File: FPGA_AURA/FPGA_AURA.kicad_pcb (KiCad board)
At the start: 8 copper layers, 50 x 50 mm, 187 parts, among them J1 ST5-40-1.00-L-D-P-TR, J100 USB_C_Receptacle_USB2.0_16P, J101 XT30PW-M, U1 XC7A35T-2FTG256C, U2 W25Q256JVEIQ, U200 ADP5014, U3 FT2232HQ, U4 TPS51200DRCR, U5 USBLC6-2SC6, U500 MT41K128M16JT-125_IT_K, U6 93LC56BT-I_SN, Y1 12MHz

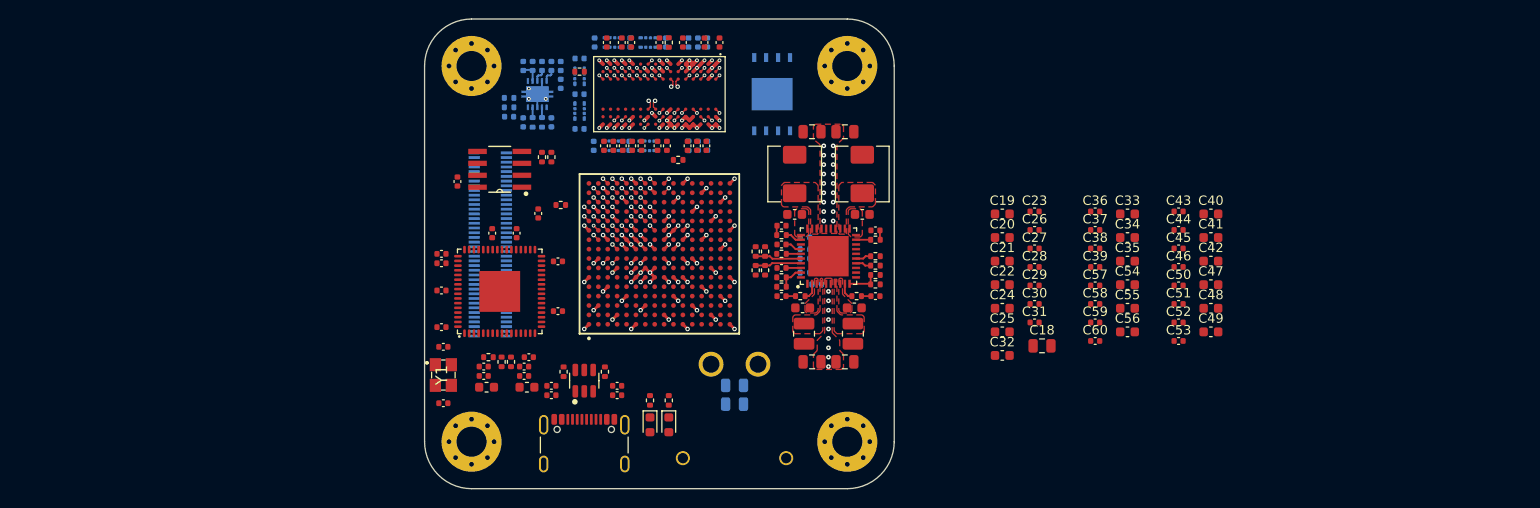
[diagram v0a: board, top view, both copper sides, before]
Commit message: Changed project philosophy
Rather than all in one, changing to an FPGA compute module which can be plugged into various boards for different functions.
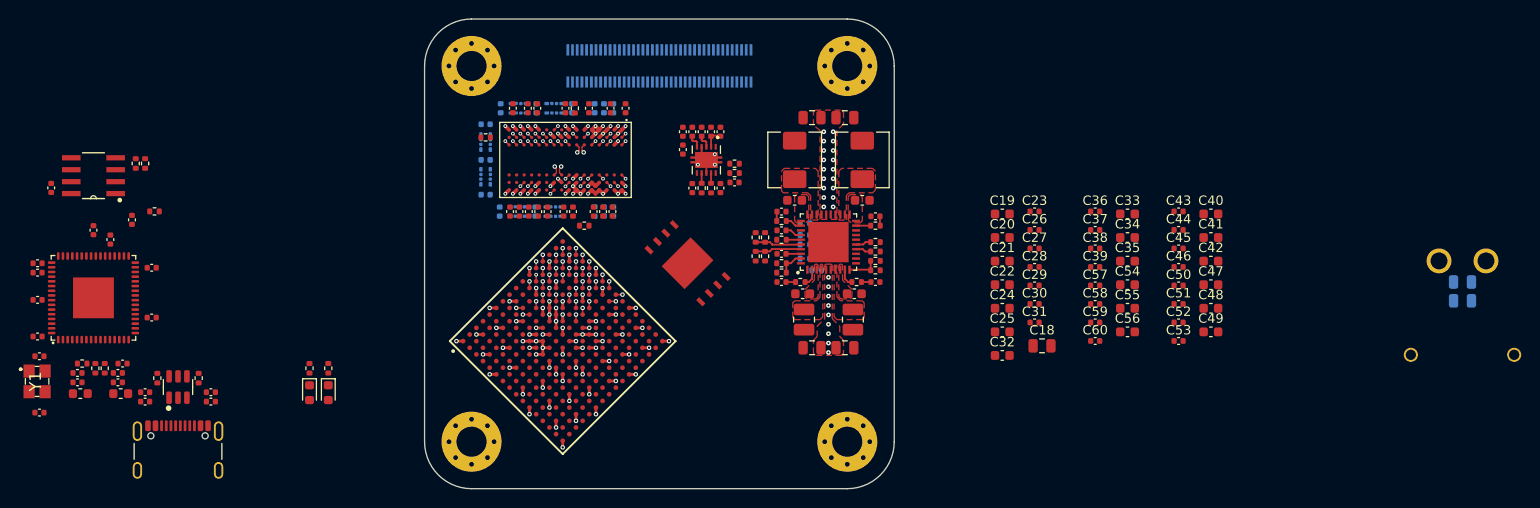
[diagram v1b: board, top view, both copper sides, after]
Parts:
- C214, C215, C216, C217, C218, C219, C221, C222, C508, R220, R221, R222, R223, U2, U4: moved to F.Cu
- moved C100 78.3 mm to (210.5, 80.0)
- moved C101 78.3 mm to (210.5, 78.0)
- moved J101 78.3 mm to (210.5, 81.8)
- moved C1 43.3 mm to (68.8, 71.4)
- moved C10 43.3 mm to (66.5, 73.5)
- moved C102 43.3 mm to (77.2, 89.7)
- moved C103 43.3 mm to (70.2, 90.7)
- moved C104 43.3 mm to (77.2, 90.7)
- moved C105 43.3 mm to (70.2, 89.7)
- moved C11 43.3 mm to (67.3, 88.7)
- moved C12 43.3 mm to (67.3, 87.7)
- moved C13 43.3 mm to (63.0, 88.7)
- moved C14 43.3 mm to (63.0, 87.7)
- moved C17 43.3 mm to (60.2, 68.0)
- moved C5 43.3 mm to (71.0, 76.5)
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
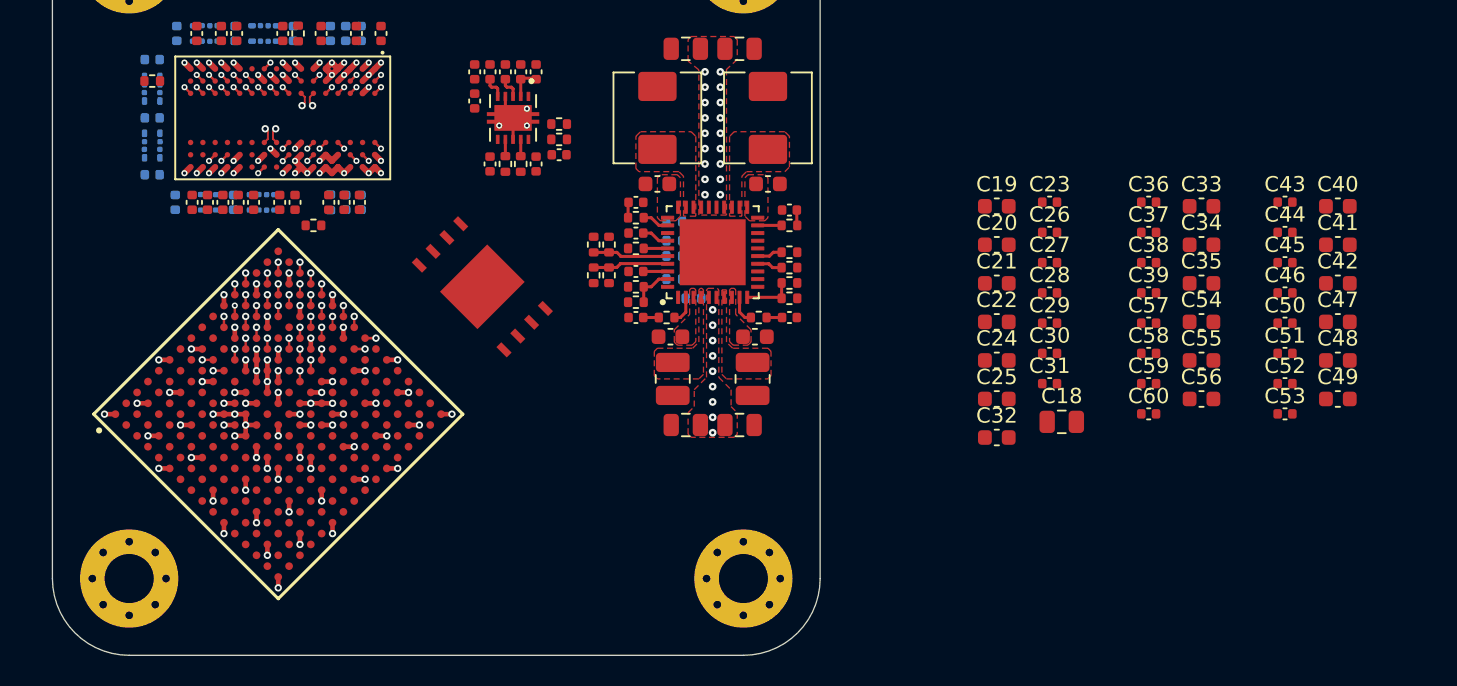
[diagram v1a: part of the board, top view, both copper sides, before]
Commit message: Started DDR routing with new layout.
All impedances setup for PCBway 8 layer stack-up.  Routing issues with the DQ lanes still to be resolved.
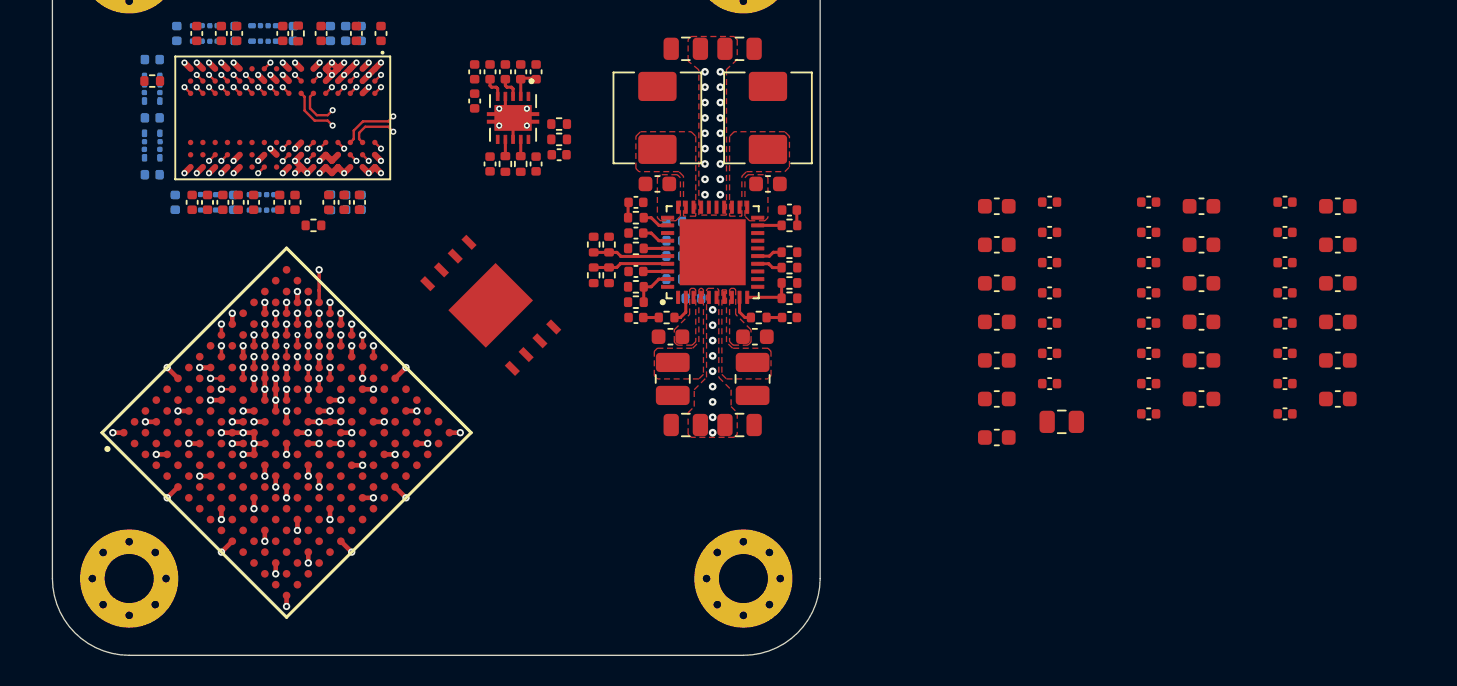
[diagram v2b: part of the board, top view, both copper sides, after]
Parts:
- moved U1 1.32 mm to (115.2, 85.5)
- moved U2 1.32 mm to (128.5, 77.2)
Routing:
- net DDR3_DQS0+: track 1.68 -> 50.4 mm
- net DDR3_DQS0-: track 1.68 -> 49.5 mm
- net DDR3_DM1: track 1.27 -> 48.0 mm
- net DDR3_DQ0: track 1.27 -> 46.4 mm
- net DDR3_DQ1: track 1.27 -> 43.6 mm
- net DDR3_DQ11: track 1.27 -> 41.2 mm
- net DDR3_DQ2: track 1.27 -> 40.0 mm
- net DDR3_DQ10: track 1.27 -> 36.9 mm
- net DDR3_DM0: track 0.57 -> 35.5 mm, vias 1 -> 2
- net DDR3_DQ8: track 1.27 -> 34.5 mm
- net DDR3_DQS1+: track 0.71 -> 29.3 mm, vias 1 -> 2
- net DDR3_DQ13: track 1.27 -> 29.7 mm
- net DDR3_DQS1-: track 0.71 -> 28.5 mm, vias 1 -> 2
- net DDR3_DQ3: track 1.27 -> 26.4 mm
- net DDR3_DQ6: track 1.27 -> 26.3 mm
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
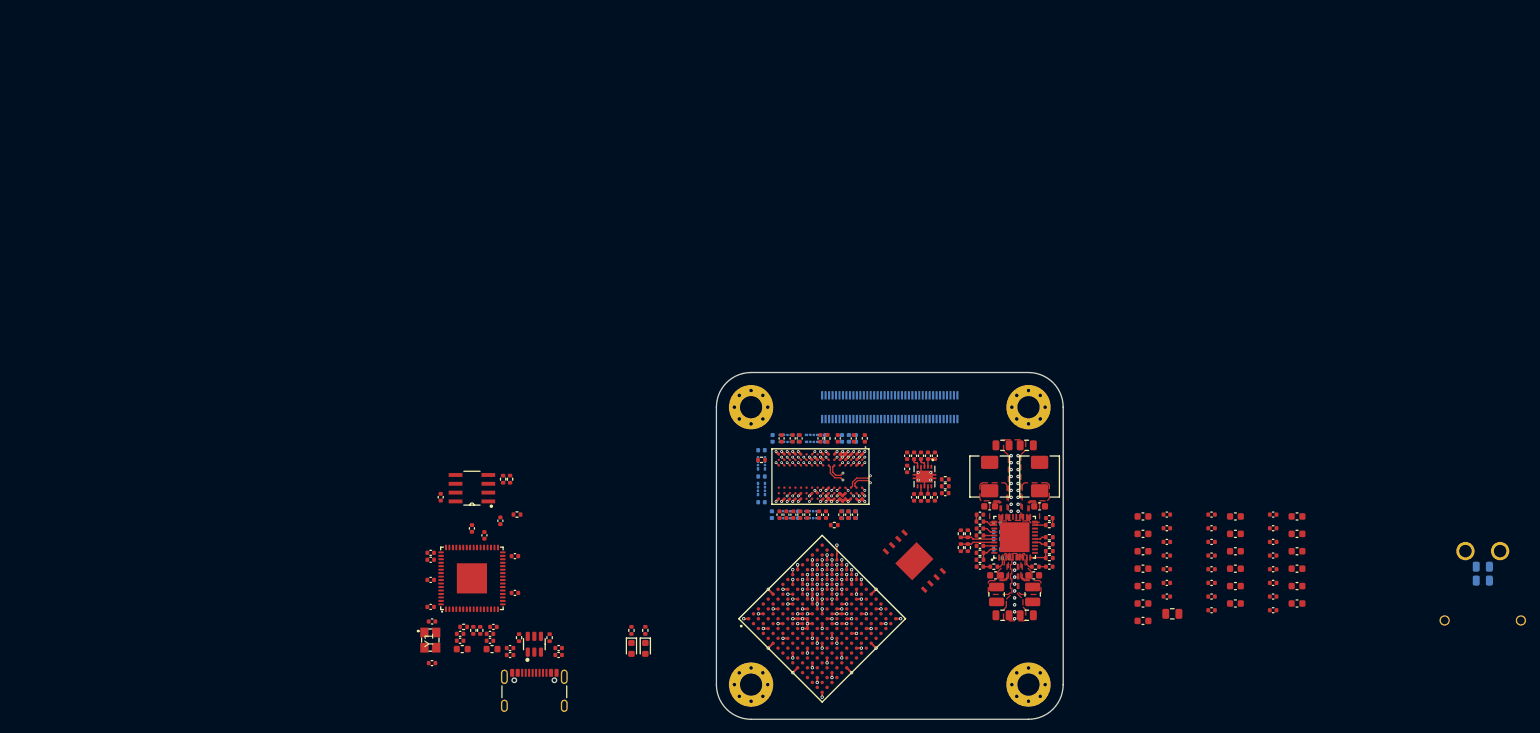
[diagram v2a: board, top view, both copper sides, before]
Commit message: DDR3 Routing complete on 3 layers, top layer left.
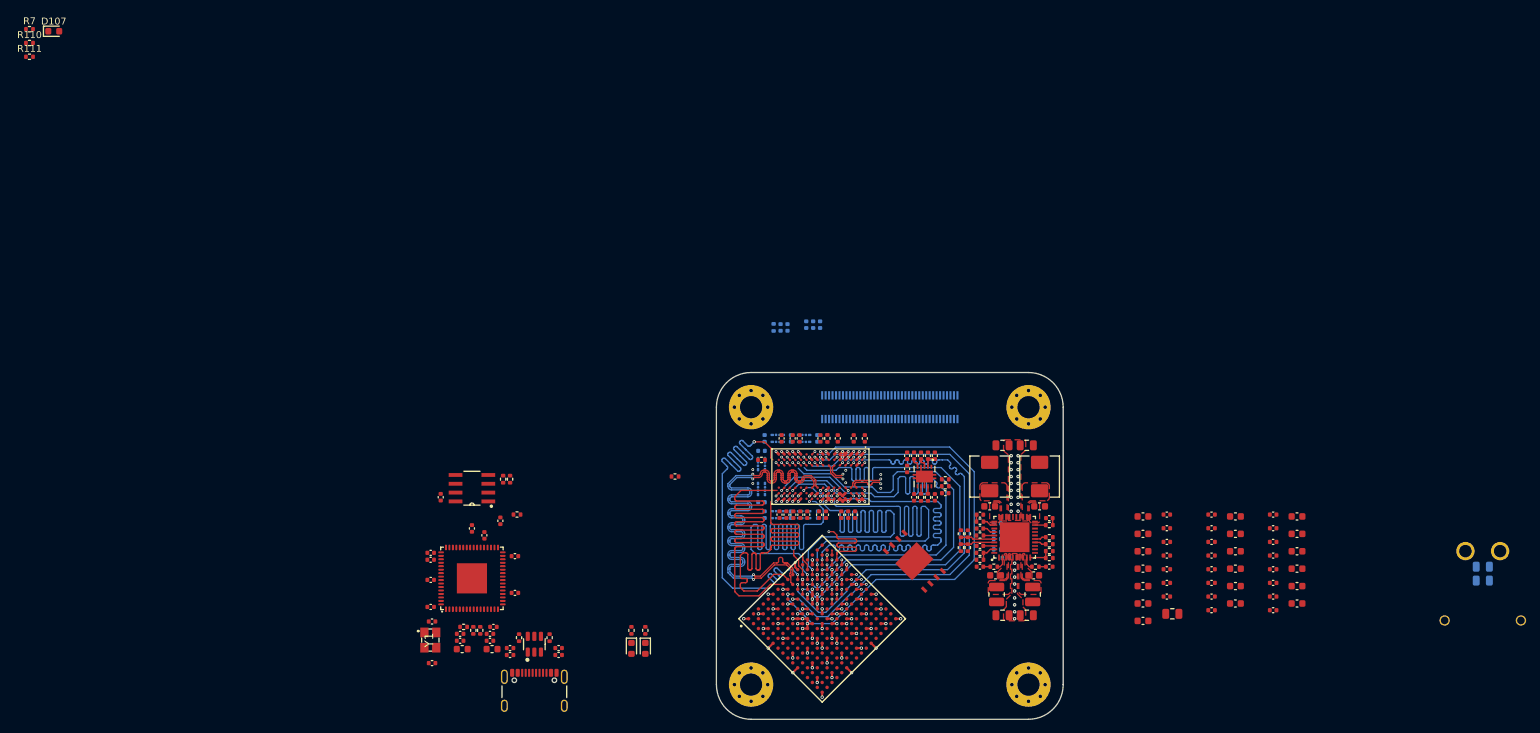
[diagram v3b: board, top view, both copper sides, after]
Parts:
- added D107: LED, LED_SMD:LED_0603_1608Metric, F.Cu at (4.46, 0.80)
- added R110: 200R, Resistor_SMD:R_0402_1005Metric, F.Cu at (0.95, 2.48)
- added R111: 100R, Resistor_SMD:R_0402_1005Metric, F.Cu at (0.95, 4.47)
- added R7: 12k, Resistor_SMD:R_0402_1005Metric, F.Cu at (0.95, 0.49)
- moved C520 28.7 mm to (109.2, 43.5)
- moved C529 28.7 mm to (110.2, 43.5)
- moved R523 28.7 mm to (108.2, 43.5)
- moved R522 24.0 mm to (94.0, 65.0)
- moved C515 17.2 mm to (115.0, 43.1)
- moved C518 17.2 mm to (113.0, 43.1)
- moved C524 17.2 mm to (114.0, 43.1)
- moved C504 9.83 mm to (114.7, 70.5), turned to 90 degrees
- moved C503 1.15 mm to (110.8, 59.5)
- moved C505 1.15 mm to (114.5, 59.5)
- moved R513 1.15 mm to (108.8, 59.5)
- moved C502 1.15 mm to (107.0, 59.5)
- moved R509 1.15 mm to (112.7, 59.5)
- moved R512 1.05 mm to (108.8, 70.5)
- moved C500 1.05 mm to (107.0, 70.5)
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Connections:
- U1 pad D11: DDR3_DQ1 -> DDR3_DQ0
- U1 pad D16: DDR3_DQ3 -> DDR3_DQ1
- U1 pad E11: DDR3_DQ0 -> DDR3_DQ2
- U1 pad E13: DDR3_DM0 -> DDR3_DQ4
- U1 pad E7: unconnected-(U1A-CFGBVS_0-PadE7) -> +3V3
- U1 pad F12: DDR3_DQ2 -> DDR3_DQ6
- U1 pad F13: DDR3_DQ6 -> DDR3_DQ3
- U1 pad F15: DDR3_DQ4 -> DDR3_DM0
- U1 pad G15: DDR3_DQ9 -> DDR3_DQ12
- U1 pad G16: DDR3_DQ14 -> DDR3_DM1
- U1 pad H10: unconnected-(U1A-DONE_0-PadH10) -> /400_FPGA_Config/DONE_0
- U1 pad H11: DDR3_DM1 -> DDR3_DQ11
- U1 pad H12: DDR3_DQ11 -> DDR3_DQ14
- U1 pad H16: DDR3_DQ15 -> DDR3_DQ9
- U1 pad H8: unconnected-(U1A-VP_0-PadH8) -> GND
- U1 pad J16: DDR3_DQ12 -> DDR3_DQ15
- U1 pad J7: unconnected-(U1A-VN_0-PadJ7) -> GND
- U1 pad K10: unconnected-(U1A-INIT_B_0-PadK10) -> /400_FPGA_Config/INIT_B_0
- U1 pad K7: unconnected-(U1A-DXN_0-PadK7) -> GND
- U1 pad K8: unconnected-(U1A-DXP_0-PadK8) -> GND
- U1 pad L13: unconnected-(U1C-IO_L5N_T0_D07_14-PadL13) -> INIT_CALIB_DONE
- U1 pad L14: unconnected-(U1C-IO_L4P_T0_D04_14-PadL14) -> TG_COMP_ERR
- U1 pad L15: unconnected-(U1A-IO_L3P_T0_DQS_PUDC_B_14-PadL15) -> GND
- U1 pad L7: unconnected-(U1A-TCK_0-PadL7) -> Net-(U1A-TCK_0)
- U1 pad M10: unconnected-(U1A-M1_0-PadM10) -> GND
- U1 pad M11: unconnected-(U1A-M2_0-PadM11) -> GND
- U1 pad M14: unconnected-(U1C-IO_L4N_T0_D05_14-PadM14) -> SYS_RST
- U1 pad M7: unconnected-(U1A-TMS_0-PadM7) -> Net-(U1A-TMS_0)
- U1 pad M9: unconnected-(U1A-M0_0-PadM9) -> +3V3
- U1 pad N11: unconnected-(U1C-IO_L13P_T2_MRCC_14-PadN11) -> 200MHz_CC_P
- U1 pad N12: unconnected-(U1C-IO_L13N_T2_MRCC_14-PadN12) -> 200MHz_CC_N
- U1 pad N7: unconnected-(U1A-TDI_0-PadN7) -> Net-(U1A-TDI_0)
- U1 pad N8: unconnected-(U1A-TDO_0-PadN8) -> Net-(U1A-TDO_0)
- U3 pad 16: unconnected-(U3-ADBUS0-Pad16) -> Net-(U1A-TCK_0)
- U3 pad 17: unconnected-(U3-ADBUS1-Pad17) -> Net-(U1A-TDI_0)
- U3 pad 18: unconnected-(U3-ADBUS2-Pad18) -> Net-(U1A-TDO_0)
- U3 pad 19: unconnected-(U3-ADBUS3-Pad19) -> Net-(U1A-TMS_0)
- U3 pad 38: unconnected-(U3-BDBUS0-Pad38) -> FTDI_TXD
- U3 pad 39: unconnected-(U3-BDBUS1-Pad39) -> FTDI_RXD
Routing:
- net DDR3_A11: track 0.00 -> 76.6 mm, vias 0 -> 1
- net DDR3_CK+: track 0.71 -> 72.7 mm, vias 1 -> 2
- net DDR3_A6: track 0.00 -> 71.6 mm, vias 0 -> 2
- net DDR3_CK-: track 0.71 -> 71.3 mm, vias 1 -> 2
- net DDR3_A7: track 1.27 -> 71.3 mm
- net DDR3_A9: track 1.27 -> 70.6 mm
- net DDR3_A2: track 1.27 -> 70.6 mm
- net DDR3_WE: track 1.27 -> 70.6 mm
- net DDR3_BA0: track 1.27 -> 70.5 mm
- net DDR3_CKE: track 1.27 -> 70.5 mm
- net DDR3_RAS: track 1.27 -> 70.1 mm
- net DDR3_A5: track 1.27 -> 66.6 mm
- net DDR3_A4: track 0.57 -> 64.4 mm, vias 1 -> 3
- net DDR3_A13: track 1.27 -> 60.6 mm
- net DDR3_A8: track 0.00 -> 58.5 mm, vias 0 -> 1
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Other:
- copper layers 8 -> 10
